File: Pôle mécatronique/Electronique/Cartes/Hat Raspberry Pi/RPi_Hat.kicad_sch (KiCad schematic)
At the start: 10 parts, among them J1 Conn_02x03_Odd_Even, U1 XBee, U2 MCP25625-x-SS, Y1 8MHz

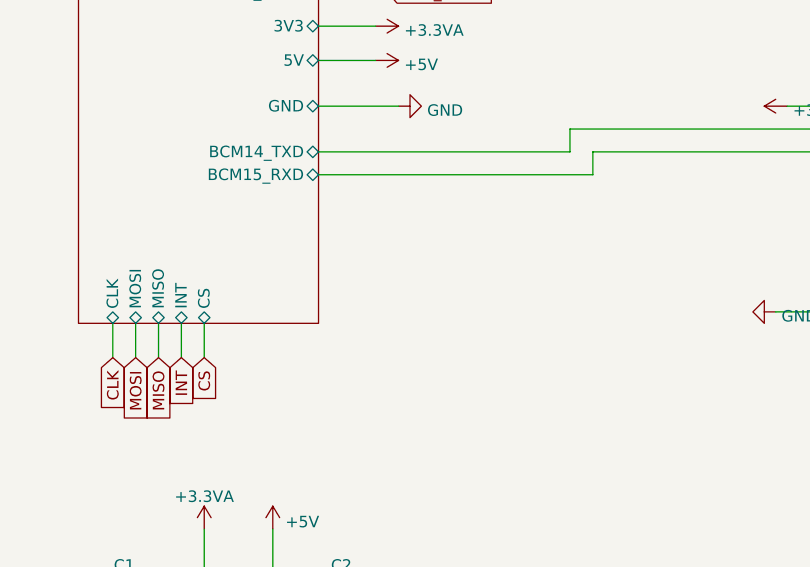
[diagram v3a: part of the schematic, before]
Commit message: Update HAT & Archi
HAT : - Ajout de l'interrupteur logique de démarrage

Archi : - Update générale
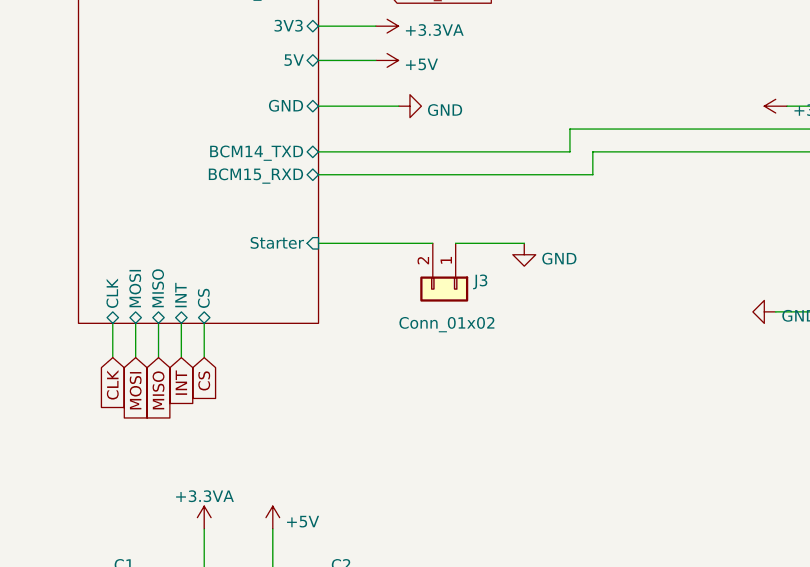
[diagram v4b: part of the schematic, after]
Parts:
- added J3: Conn_01x02, Connector_JST:JST_PH_B2B-PH-K_1x02_P2.00mm_Vertical, symbol Connector_Generic:Conn_01x02
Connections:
- net GND: now also J3.1 (Pin_1)
- new net RPi_GPIO/Starter: J3.2 (Pin_2)
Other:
- sheet RPi_GPIO ports: added Starter; removed none
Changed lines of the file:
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@@
+    (stroke (width 0) (type default) (color 0 0 0 0))
+  )
+  (wire (pts (xy 128.27 63.5) (xy 140.97 63.5))
     (stroke (width 0) (type default) (color 0 0 0 0))
   )
@@
   )
   (wire (pts (xy 118.11 167.64) (xy 118.11 171.45))
+    (stroke (width 0) (type default) (color 0 0 0 0))
+  )
+  (wire (pts (xy 143.51 63.5) (xy 151.13 63.5))
     (stroke (width 0) (type default) (color 0 0 0 0))
   )
@@
     )
     (pin "1")
+  )
+  (symbol (lib_id "Connector_Generic:Conn_01x02") (at 143.51 68.58 270) (unit 1)
+    (in_bom yes) (on_board yes)
+    (property "Reference" "J3" (id 0) (at 145.542 67.6715 90)
+      (effects (font (size 1.27 1.27)) (justify left))
+    )
+    (property "Value" "Conn_01x02" (id 1) (at 137.16 72.39 90)
+      (effects (font (size 1.27 1.27)) (justify left))
+    )
+    (property "Footprint" "Connector_JST:JST_PH_B2B-PH-K_1x02_P2.00mm_Vertical" (id 2) (at 143.51 68.58 0)
+      (effects (font (size 1.27 1.27)) hide)
+    )
+    (property "Datasheet" "~" (id 3) (at 143.51 68.58 0)
+      (effects (font (size 1.27 1.27)) hide)
+    )
+    (pin "1")
+    (pin "2")
   )
   (symbol (lib_id "Device:R") (at 201.93 125.73 180) (unit 1)
@@
     )
     (property "Datasheet" "" (id 3) (at 118.11 171.45 0)
+      (effects (font (size 1.27 1.27)) hide)
+    )
+    (pin "1")
+  )
+  (symbol (lib_id "power:GND") (at 151.13 63.5 0) (unit 1)
+    (in_bom yes) (on_board yes) (fields_autoplaced)
+    (property "Reference" "#PWR0115" (id 0) (at 151.13 69.85 0)
+      (effects (font (size 1.27 1.27)) hide)
+    )
+    (property "Value" "GND" (id 1) (at 153.035 65.249 0)
+      (effects (font (size 1.27 1.27)) (justify left))
+    )
+    (property "Footprint" "" (id 2) (at 151.13 63.5 0)
+      (effects (font (size 1.27 1.27)) hide)
+    )
+    (property "Datasheet" "" (id 3) (at 151.13 63.5 0)
       (effects (font (size 1.27 1.27)) hide)
     )
@@
       (effects (font (size 1.27 1.27)) (justify left))
     )
+    (pin "Starter" input (at 128.27 63.5 0)
+      (effects (font (size 1.27 1.27)) (justify right))
+    )
   )
   (sheet_instances
@@
       (reference "#PWR0114") (unit 1) (value "+5V") (footprint "")
     )
+    (path "/90db120d-54ee-4b43-8cda-173023286d38"
+      (reference "#PWR0115") (unit 1) (value "GND") (footprint "")
+    )
     (path "/af20f0d1-11f6-45b0-988d-d58837807af5"
       (reference "C1") (unit 1) (value "100 nF") (footprint "Capacitor_THT:C_Disc_D5.1mm_W3.2mm_P5.00mm")
@@
       (reference "J2") (unit 1) (value "RPi_GPIO") (footprint "RPi_Hat:Pin_Header_Straight_2x20")
     )
+    (path "/51b5800b-b46a-41ae-9828-338530f43dcd"
+      (reference "J3") (unit 1) (value "Conn_01x02") (footprint "Connector_JST:JST_PH_B2B-PH-K_1x02_P2.00mm_Vertical")
+    )
     (path "/5d503d09-3382-41b1-85dd-a984512b456d"
